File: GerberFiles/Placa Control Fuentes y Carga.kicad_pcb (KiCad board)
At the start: 2 copper layers, 160 x 95 mm, 139 parts, among them J1 TBP01R1-508-02BE, J10 TBP01R1-508-03BE, J2 TBP01R1-508-02BE, J3 TBP01R1-508-02BE, J4 TBP01R1-508-02BE, J5 TBP01R1-508-02BE, J6 TBP01R1-508-02BE, J7 TBP01R1-508-02BE, J8 TBP01R1-508-02BE, J9 TBP01R1-508-02BE, Q1 IRF9540N, Q2 2N3904, Q3 BC558, Q4 BC558, Q5 IRF5305, Q6 BC337, Q7 BC327, U1 ACS724LLCTR-05AB-T, U2 Relay_Module_WB-083, U3 4N35, U4 LM2596S_Modulo_Regulable, U5 Arduino_Nano_ATmega328P, U6 ACS724LLCTR-05AB-T, U7 MAX485E, U8 MAX22445FAWE+, U9 RI3-0505S

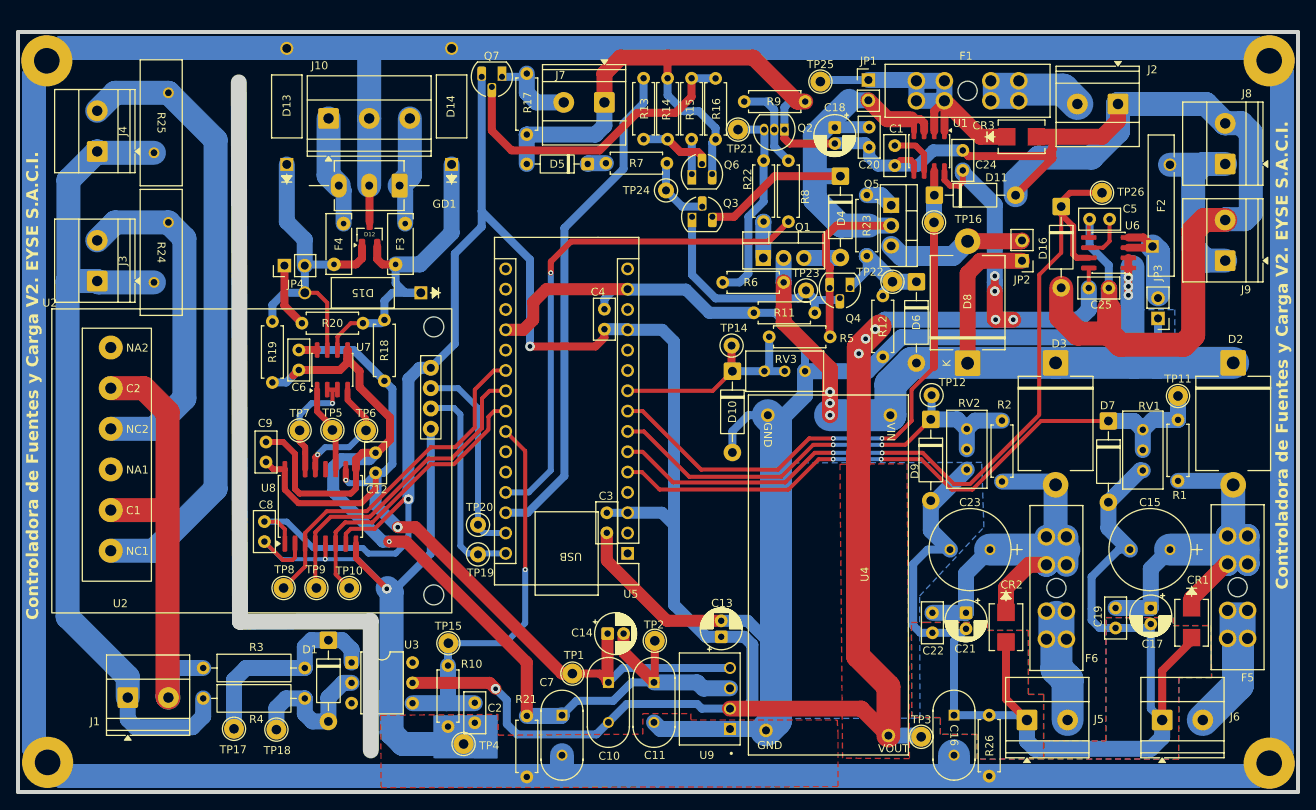
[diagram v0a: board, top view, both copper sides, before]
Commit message: Se le agregó el conector con las señales de +5V, GND, ADC0 y apagadoTX para la plaqueita adicional de corte de TX que irá apilada encima con dos tornillos de 1/8 para sujeción mecánica arriba del arduino nano. Se hicieron los gerbers files, se agregó el conecto a la lista de materiales y se le envió a "compras" para su fabricación. Ya se dá por finalizada una primer etapa del proyecto.
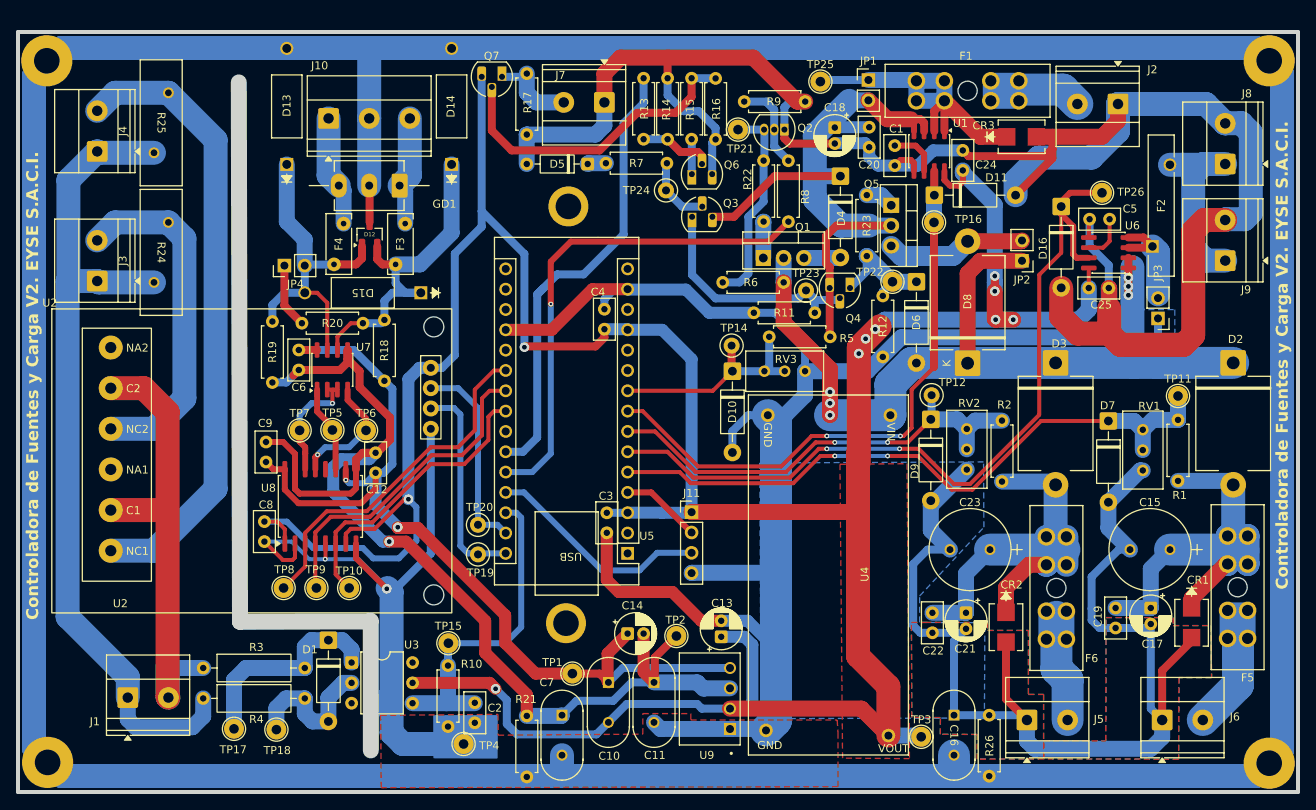
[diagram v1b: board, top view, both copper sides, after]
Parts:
- added H5: MountingHole_Pad, MountingHole:MountingHole_3.2mm_M3_Pad, F.Cu at (129.0, 128.9)
- added H6: MountingHole_Pad, MountingHole:MountingHole_3.2mm_M3_Pad, F.Cu at (129.3, 76.8)
- added J11: Conn_01x04, Connector_PinHeader_2.54mm:PinHeader_1x04_P2.54mm_Vertical, F.Cu at (144.7, 115.0)
- moved TP2 2.77 mm to (142.8, 130.5)
- moved C14 2.50 mm to (136.7, 130.2)
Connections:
- U5 pad 24: F220_IN -> unconnected-(U5-D6-Pad24)
- U5 pad 25: unconnected-(U5-D7-Pad25) -> F220_OUT
- U5 pad 26: unconnected-(U5-D8-Pad26) -> PWM
- U5 pad 27: PWM -> apagadoTX
- U5 pad 28: F220_OUT -> F220_IN
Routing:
- net apagadoTX: track 0.00 -> 28.2 mm
- net GND: track 684.6 -> 695.4 mm
- net ADC0: track 0.00 -> 10.2 mm
- net F220_IN: track 51.1 -> 41.3 mm, vias 1 -> 0
- net +5V: track 395.0 -> 402.7 mm
- net F220_OUT: track 63.1 -> 58.2 mm
- net +5V_B: track 118.2 -> 121.3 mm
- net PWM: track 64.6 -> 62.4 mm
- net RO: track 36.2 -> 36.9 mm
- net GND_B: track 141.2 -> 141.9 mm
- net DI: track 40.3 -> 40.8 mm
